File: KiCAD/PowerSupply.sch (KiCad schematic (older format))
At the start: 12 parts, among them J1 USBAB, Q1 3.7A/20V, U1 LM1117-5.0, U2 AP2112K-3.3

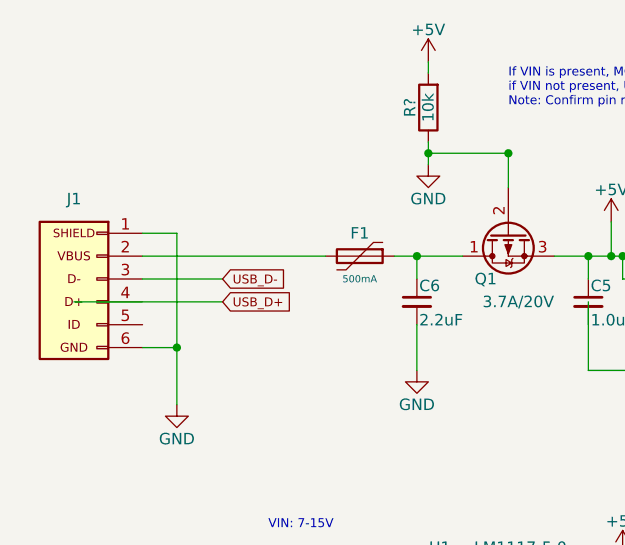
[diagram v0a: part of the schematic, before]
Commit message: Broke out pins from MCU and added data bus protection diode
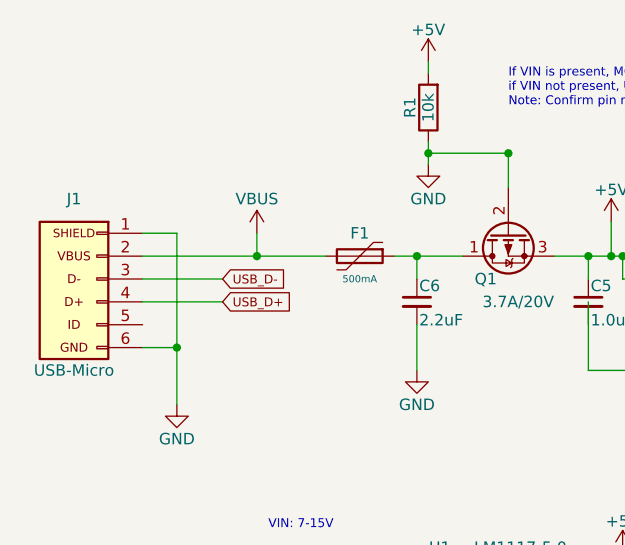
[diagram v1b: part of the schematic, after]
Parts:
- J1: value USBAB -> USB-Micro
- gave numbers to parts that had none: 1
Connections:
- net labels added: VBUS
- wire segments 36 -> 37
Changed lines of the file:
@@
 $EndDescr
 $Comp
-L GND #PWR?
+L GND #PWR201
 U 1 1 5BF271E8
 P 4600 4100
-F 0 "#PWR?" H 4600 3850 50  0001 C CNN
+F 0 "#PWR201" H 4600 3850 50  0001 C CNN
 F 1 "GND" H 4600 3950 50  0000 C CNN
 F 2 "" H 4600 4100 50  0001 C CNN
@@
 $EndComp
 $Comp
-L R R?
+L R R1
 U 1 1 5BF27207
 P 5700 2800
-F 0 "R?" V 5780 2800 50  0000 C CNN
+F 0 "R1" V 5780 2800 50  0000 C CNN
 F 1 "10k" V 5700 2800 50  0000 C CNN
 F 2 "" V 5630 2800 50  0001 C CNN
@@
 $EndComp
 $Comp
-L GND #PWR?
+L GND #PWR205
 U 1 1 5BF2720F
 P 5700 3050
-F 0 "#PWR?" H 5700 2800 50  0001 C CNN
+F 0 "#PWR205" H 5700 2800 50  0001 C CNN
 F 1 "GND" H 5700 2900 50  0000 C CNN
 F 2 "" H 5700 3050 50  0001 C CNN
@@
 VIN
 $Comp
-L +5V #PWR?
+L +5V #PWR204
 U 1 1 5BF27217
 P 5700 2600
-F 0 "#PWR?" H 5700 2450 50  0001 C CNN
+F 0 "#PWR204" H 5700 2450 50  0001 C CNN
 F 1 "+5V" H 5700 2740 50  0000 C CNN
 F 2 "" H 5700 2600 50  0001 C CNN
@@
 P 4150 3550
 F 0 "J1" H 4150 3900 50  0000 C CNN
-F 1 "USBAB" H 4150 3150 50  0001 C CNN
+F 1 "USB-Micro" H 4150 3150 50  0000 C CNN
 F 2 "" H 4250 3550 50  0001 C CNN
 F 3 "" H 4250 3550 50  0001 C CNN
@@
 VIN: 7-15V
 $Comp
-L GND #PWR?
+L GND #PWR206
 U 1 1 5BF27ED3
 P 5900 5250
-F 0 "#PWR?" H 5900 5000 50  0001 C CNN
+F 0 "#PWR206" H 5900 5000 50  0001 C CNN
 F 1 "GND" H 5900 5100 50  0000 C CNN
 F 2 "" H 5900 5250 50  0001 C CNN
@@
 $EndComp
 $Comp
-L +5V #PWR?
+L +5V #PWR208
 U 1 1 5BF285D5
 P 6550 4750
-F 0 "#PWR?" H 6550 4600 50  0001 C CNN
+F 0 "#PWR208" H 6550 4600 50  0001 C CNN
 F 1 "+5V" H 6550 4890 50  0000 C CNN
 F 2 "" H 6550 4750 50  0001 C CNN
@@
 $EndComp
 $Comp
-L GND #PWR?
+L GND #PWR209
 U 1 1 5BF28EA0
 P 6950 3950
-F 0 "#PWR?" H 6950 3700 50  0001 C CNN
+F 0 "#PWR209" H 6950 3700 50  0001 C CNN
 F 1 "GND" H 6950 3800 50  0000 C CNN
 F 2 "" H 6950 3950 50  0001 C CNN
@@
 $EndComp
 $Comp
-L +3.3V #PWR?
+L +3.3V #PWR210
 U 1 1 5BF2913F
 P 7600 3350
-F 0 "#PWR?" H 7600 3200 50  0001 C CNN
+F 0 "#PWR210" H 7600 3200 50  0001 C CNN
 F 1 "+3.3V" H 7600 3490 50  0000 C CNN
 F 2 "" H 7600 3350 50  0001 C CNN
@@
 	1    0    0    -1
 $EndComp
-Wire Wire Line
-	4600 3350 4600 4100
-Wire Wire Line
-	4450 3850 4600 3850
-Wire Wire Line
-	4450 3350 4600 3350
-Connection ~ 4600 3850
-Wire Wire Line
-	4150 3650 4800 3650
-Wire Wire Line
-	4450 3450 5250 3450
-Wire Wire Line
-	5550 3450 5850 3450
-Wire Wire Line
-	6050 3000 6050 3150
-Connection ~ 6050 3000
-Wire Wire Line
-	5700 2950 5700 3050
-Wire Wire Line
-	5700 2650 5700 2600
-Wire Wire Line
-	6050 3000 5700 3000
-Connection ~ 5700 3000
-Wire Wire Line
-	4450 3550 4800 3550
-Wire Wire Line
-	5150 4850 5600 4850
-Wire Wire Line
-	5900 5250 5900 5150
-Wire Wire Line
-	5450 5100 5450 5200
-Wire Wire Line
-	5450 5200 6700 5200
-Connection ~ 5900 5200
-Wire Wire Line
-	5450 4900 5450 4850
-Connection ~ 5450 4850
-Wire Wire Line
-	6400 5200 6400 5100
-Wire Wire Line
-	6200 4850 6700 4850
-Wire Wire Line
-	6400 4850 6400 4900
-Wire Wire Line
-	6700 5200 6700 5100
-Connection ~ 6400 5200
-Wire Wire Line
-	6700 4850 6700 4900
-Connection ~ 6400 4850
-Wire Wire Line
-	6550 4850 6550 4750
-Connection ~ 6550 4850
-Wire Wire Line
-	7250 3450 7750 3450
-Wire Wire Line
-	6950 3950 6950 3850
-Wire Wire Line
-	6400 3950 7750 3950
-Wire Wire Line
-	6250 3450 6650 3450
-Wire Wire Line
-	6650 3550 6550 3550
-Wire Wire Line
-	6550 3550 6550 3450
-Connection ~ 6550 3450
-Wire Wire Line
-	6400 3650 6400 3950
-Connection ~ 6950 3950
-Wire Wire Line
-	7750 3950 7750 3650
-Wire Wire Line
-	7600 3350 7600 3450
-Connection ~ 7600 3450
 $Comp
 L C_Small C6
@@
 	1    0    0    -1
 $EndComp
-Wire Wire Line
-	7750 3450 7750 3550
-Wire Wire Line
-	6400 3550 6400 3450
-Connection ~ 6400 3450
-Wire Wire Line
-	5650 3550 5650 3450
-Connection ~ 5650 3450
-$Comp
-L GND #PWR?
+$Comp
+L GND #PWR203
 U 1 1 5BF29400
 P 5650 3950
-F 0 "#PWR?" H 5650 3700 50  0001 C CNN
+F 0 "#PWR203" H 5650 3700 50  0001 C CNN
 F 1 "GND" H 5650 3800 50  0000 C CNN
 F 2 "" H 5650 3950 50  0001 C CNN
@@
 	1    0    0    -1
 $EndComp
-Wire Wire Line
-	5650 3950 5650 3750
-$Comp
-L +5V #PWR?
+$Comp
+L +5V #PWR207
 U 1 1 5BF2A2B6
 P 6500 3300
-F 0 "#PWR?" H 6500 3150 50  0001 C CNN
+F 0 "#PWR207" H 6500 3150 50  0001 C CNN
 F 1 "+5V" H 6500 3440 50  0000 C CNN
 F 2 "" H 6500 3300 50  0001 C CNN
@@
 	1    0    0    -1
 $EndComp
-Wire Wire Line
-	6500 3300 6500 3450
-Connection ~ 6500 3450
 Text Notes 6050 2800 0    39   ~ 0
 If VIN is present, MOSFET will not conduct\nif VIN not present, USB_VBUS will flow through Q1\nNote: Confirm pin numbering with part
+$Comp
+L VBUS #PWR202
+U 1 1 5BF2FD1D
+P 4950 3350
+F 0 "#PWR202" H 4950 3200 50  0001 C CNN
+F 1 "VBUS" H 4950 3500 50  0000 C CNN
+F 2 "" H 4950 3350 50  0001 C CNN
+F 3 "" H 4950 3350 50  0001 C CNN
+	1    4950 3350
+	1    0    0    -1
+$EndComp
+Wire Wire Line
+	6400 3650 6400 3950
+Connection ~ 4950 3450
+Wire Wire Line
+	4950 3350 4950 3450
+Wire Wire Line
+	4450 3650 4800 3650
+Connection ~ 6500 3450
+Wire Wire Line
+	6500 3300 6500 3450
+Wire Wire Line
+	5650 3950 5650 3750
+Connection ~ 5650 3450
+Wire Wire Line
+	5650 3550 5650 3450
+Connection ~ 6400 3450
+Wire Wire Line
+	6400 3550 6400 3450
+Wire Wire Line
+	7750 3450 7750 3550
+Connection ~ 7600 3450
+Wire Wire Line
+	7600 3350 7600 3450
+Wire Wire Line
+	7750 3950 7750 3650
+Connection ~ 6950 3950
+Connection ~ 6550 3450
+Wire Wire Line
+	6550 3550 6550 3450
+Wire Wire Line
+	6650 3550 6550 3550
+Wire Wire Line
+	6250 3450 6650 3450
+Wire Wire Line
+	6400 3950 7750 3950
+Wire Wire Line
+	6950 3950 6950 3850
+Wire Wire Line
+	7250 3450 7750 3450
+Connection ~ 6550 4850
+Wire Wire Line
+	6550 4850 6550 4750
+Connection ~ 6400 4850
+Wire Wire Line
+	6700 4850 6700 4900
+Connection ~ 6400 5200
+Wire Wire Line
+	6700 5200 6700 5100
+Wire Wire Line
+	6400 4850 6400 4900
+Wire Wire Line
+	6200 4850 6700 4850
+Wire Wire Line
+	6400 5200 6400 5100
+Connection ~ 5450 4850
+Wire Wire Line
+	5450 4900 5450 4850
+Connection ~ 5900 5200
+Wire Wire Line
+	5450 5200 6700 5200
+Wire Wire Line
+	5450 5100 5450 5200
+Wire Wire Line
+	5900 5250 5900 5150
+Wire Wire Line
+	5150 4850 5600 4850
+Wire Wire Line
+	4450 3550 4800 3550
+Connection ~ 5700 3000
+Wire Wire Line
+	6050 3000 5700 3000
+Wire Wire Line
+	5700 2650 5700 2600
+Wire Wire Line
+	5700 2950 5700 3050
+Connection ~ 6050 3000
+Wire Wire Line
+	6050 3000 6050 3150
+Wire Wire Line
+	5550 3450 5850 3450
+Wire Wire Line
+	4450 3450 5250 3450
+Connection ~ 4600 3850
+Wire Wire Line
+	4450 3350 4600 3350
+Wire Wire Line
+	4450 3850 4600 3850
+Wire Wire Line
+	4600 3350 4600 4100
 $EndSCHEMATC

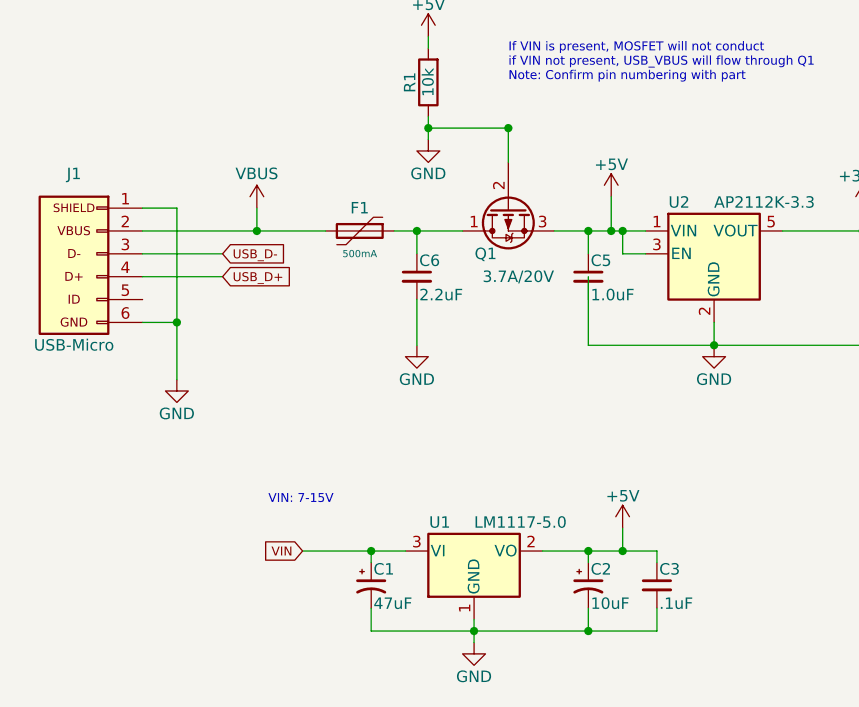
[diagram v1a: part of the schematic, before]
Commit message: Editing capacitor values, prepping for layout phase
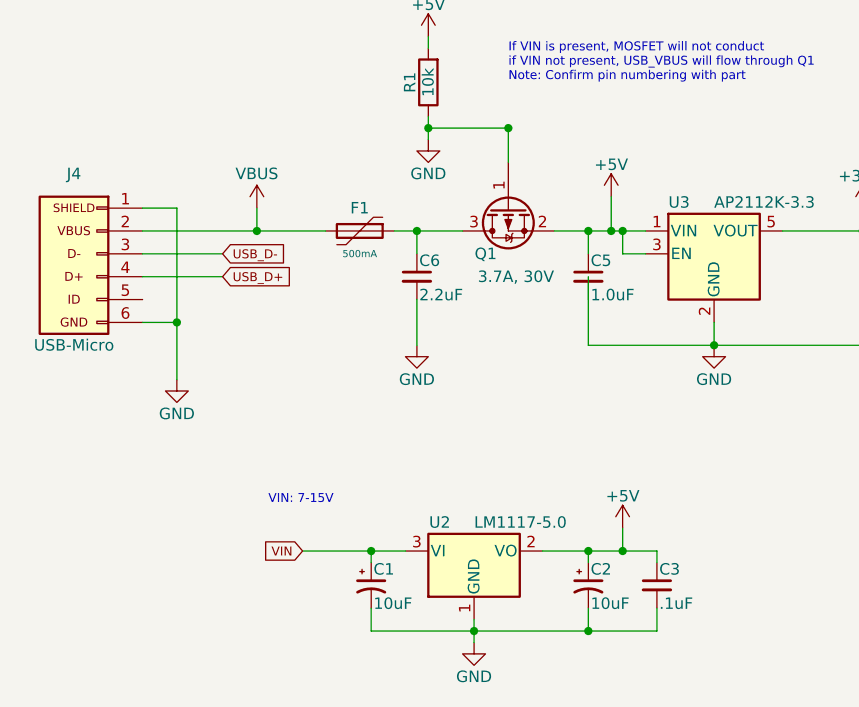
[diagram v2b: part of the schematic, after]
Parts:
- removed Q1: 3.7A/20V, symbol Q_PMOS_DGS
- added Q1: 3.7A, 30V, symbol Q_PMOS_GSD
- C1: value 47uF -> 10uF
- renumbered J1 to J4, U1 to U2, U2 to U3
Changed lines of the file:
@@
 LIBS:MF-MSMF050-2
 LIBS:AP2112K-3.3TRG1
+LIBS:cortex_debug
+LIBS:B3FS-4005P
 LIBS:SAMD21-DevBoard-cache
 EELAYER 25 0
@@
 $EndComp
 $Comp
-L Q_PMOS_DGS Q1
-U 1 1 5BF271FF
-P 6050 3350
-F 0 "Q1" V 6250 3400 50  0000 L CNN
-F 1 "3.7A/20V" V 6350 3150 50  0000 L CNN
-F 2 "" H 6250 3450 50  0001 C CNN
-F 3 "" H 6050 3350 50  0001 C CNN
-	1    6050 3350
-	0    -1   1    0
-$EndComp
-$Comp
 L R R1
 U 1 1 5BF27207
@@
 $EndComp
 $Comp
-L USBAB J1
+L USBAB J4
 U 1 1 5BF271E1
 P 4150 3550
-F 0 "J1" H 4150 3900 50  0000 C CNN
+F 0 "J4" H 4150 3900 50  0000 C CNN
 F 1 "USB-Micro" H 4150 3150 50  0000 C CNN
 F 2 "" H 4250 3550 50  0001 C CNN
@@
 $EndComp
 $Comp
-L LM1117-5.0 U1
+L LM1117-5.0 U2
 U 1 1 5BF2791A
 P 5900 4850
-F 0 "U1" H 5750 4975 50  0000 C CNN
+F 0 "U2" H 5750 4975 50  0000 C CNN
 F 1 "LM1117-5.0" H 5900 4975 50  0000 L CNN
 F 2 "" H 5900 4850 50  0001 C CNN
@@
 P 5450 5000
 F 0 "C1" H 5460 5070 50  0000 L CNN
-F 1 "47uF" H 5460 4920 50  0000 L CNN
+F 1 "10uF" H 5460 4920 50  0000 L CNN
 F 2 "" H 5450 5000 50  0001 C CNN
 F 3 "" H 5450 5000 50  0001 C CNN
@@
 $EndComp
 $Comp
-L AP2112K-3.3 U2
+L AP2112K-3.3 U3
 U 1 1 5BF28D97
 P 6950 3550
-F 0 "U2" H 6750 3775 50  0000 L CNN
+F 0 "U3" H 6750 3775 50  0000 L CNN
 F 1 "AP2112K-3.3" H 6950 3775 50  0000 L CNN
 F 2 "TO_SOT_Packages_SMD:SOT-23-5" H 6950 3875 50  0001 C CNN
@@
 Wire Wire Line
 	4600 3350 4600 4100
+$Comp
+L Q_PMOS_GSD Q1
+U 1 1 5C02D8EB
+P 6050 3350
+F 0 "Q1" V 6250 3400 50  0000 L CNN
+F 1 "3.7A, 30V" V 6350 3150 50  0000 L CNN
+F 2 "" H 6250 3450 50  0001 C CNN
+F 3 "" H 6050 3350 50  0001 C CNN
+	1    6050 3350
+	0    -1   1    0
+$EndComp
 $EndSCHEMATC

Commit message: Created footprints for switch, micro usb port and crystal
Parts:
- C1, C2, C3: footprint (none) -> Capacitors_SMD:C_1206
- C4, C5, C6: footprint (none) -> Capacitors_SMD:C_1210
- F1, R1: footprint (none) -> Resistors_SMD:R_1210
- J4: footprint (none) -> 10118192-0001LF:10118192-0001LF
- Q1: footprint (none) -> TO_SOT_Packages_SMD:SOT-23
- U2: footprint (none) -> TO_SOT_Packages_SMD:SOT-223
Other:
- note added: "0"
- note added: "12/2/18"
- note added: "Author: Matthew Cox\nOrganization: University of Connecticut Formula SAE"
- note added: "If VIN is present, MOSFET will not conduct\nif VIN not present, USB_VBUS will flow through Q1"
- note added: "SAMD21 Dev Board - Power Supply"
- note removed: "If VIN is present, MOSFET will not conduct\nif VIN not present, USB_VBUS will flow through Q1\nNote: Confirm pin numbering with part"
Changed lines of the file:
@@
 $EndDescr
 $Comp
-L GND #PWR201
+L GND #PWR027
 U 1 1 5BF271E8
-P 4600 4100
-F 0 "#PWR201" H 4600 3850 50  0001 C CNN
-F 1 "GND" H 4600 3950 50  0000 C CNN
-F 2 "" H 4600 4100 50  0001 C CNN
-F 3 "" H 4600 4100 50  0001 C CNN
-	1    4600 4100
+P 4600 3950
+F 0 "#PWR027" H 4600 3700 50  0001 C CNN
+F 1 "GND" H 4600 3800 50  0000 C CNN
+F 2 "" H 4600 3950 50  0001 C CNN
+F 3 "" H 4600 3950 50  0001 C CNN
+	1    4600 3950
 	1    0    0    -1
 $EndComp
@@
 F 0 "F1" V 5300 3450 50  0000 C CNN
 F 1 "500mA" V 5500 3450 31  0000 C CNN
-F 2 "" H 5450 3250 50  0001 L CNN
+F 2 "Resistors_SMD:R_1210" H 5450 3250 50  0001 L CNN
 F 3 "" H 5400 3450 50  0001 C CNN
 	1    5400 3450
@@
 F 0 "R1" V 5780 2800 50  0000 C CNN
 F 1 "10k" V 5700 2800 50  0000 C CNN
-F 2 "" V 5630 2800 50  0001 C CNN
+F 2 "Resistors_SMD:R_1210" V 5630 2800 50  0001 C CNN
 F 3 "" H 5700 2800 50  0001 C CNN
 	1    5700 2800
@@
 $EndComp
 $Comp
-L GND #PWR205
+L GND #PWR028
 U 1 1 5BF2720F
 P 5700 3050
-F 0 "#PWR205" H 5700 2800 50  0001 C CNN
+F 0 "#PWR028" H 5700 2800 50  0001 C CNN
 F 1 "GND" H 5700 2900 50  0000 C CNN
 F 2 "" H 5700 3050 50  0001 C CNN
@@
 VIN
 $Comp
-L +5V #PWR204
+L +5V #PWR029
 U 1 1 5BF27217
 P 5700 2600
-F 0 "#PWR204" H 5700 2450 50  0001 C CNN
+F 0 "#PWR029" H 5700 2450 50  0001 C CNN
 F 1 "+5V" H 5700 2740 50  0000 C CNN
 F 2 "" H 5700 2600 50  0001 C CNN
@@
 F 0 "J4" H 4150 3900 50  0000 C CNN
 F 1 "USB-Micro" H 4150 3150 50  0000 C CNN
-F 2 "" H 4250 3550 50  0001 C CNN
+F 2 "10118192-0001LF:10118192-0001LF" H 4250 3550 50  0001 C CNN
 F 3 "" H 4250 3550 50  0001 C CNN
 	1    4150 3550
@@
 F 0 "U2" H 5750 4975 50  0000 C CNN
 F 1 "LM1117-5.0" H 5900 4975 50  0000 L CNN
-F 2 "" H 5900 4850 50  0001 C CNN
+F 2 "TO_SOT_Packages_SMD:SOT-223" H 5900 4850 50  0001 C CNN
 F 3 "" H 5900 4850 50  0001 C CNN
 	1    5900 4850
@@
 VIN: 7-15V
 $Comp
-L GND #PWR206
+L GND #PWR030
 U 1 1 5BF27ED3
 P 5900 5250
-F 0 "#PWR206" H 5900 5000 50  0001 C CNN
+F 0 "#PWR030" H 5900 5000 50  0001 C CNN
 F 1 "GND" H 5900 5100 50  0000 C CNN
 F 2 "" H 5900 5250 50  0001 C CNN
@@
 F 0 "C1" H 5460 5070 50  0000 L CNN
 F 1 "10uF" H 5460 4920 50  0000 L CNN
-F 2 "" H 5450 5000 50  0001 C CNN
+F 2 "Capacitors_SMD:C_1206" H 5450 5000 50  0001 C CNN
 F 3 "" H 5450 5000 50  0001 C CNN
 	1    5450 5000
@@
 F 0 "C2" H 6410 5070 50  0000 L CNN
 F 1 "10uF" H 6410 4920 50  0000 L CNN
-F 2 "" H 6400 5000 50  0001 C CNN
+F 2 "Capacitors_SMD:C_1206" H 6400 5000 50  0001 C CNN
 F 3 "" H 6400 5000 50  0001 C CNN
 	1    6400 5000
@@
 F 0 "C3" H 6710 5070 50  0000 L CNN
 F 1 ".1uF" H 6710 4920 50  0000 L CNN
-F 2 "" H 6700 5000 50  0001 C CNN
+F 2 "Capacitors_SMD:C_1206" H 6700 5000 50  0001 C CNN
 F 3 "" H 6700 5000 50  0001 C CNN
 	1    6700 5000
@@
 $EndComp
 $Comp
-L +5V #PWR208
+L +5V #PWR031
 U 1 1 5BF285D5
 P 6550 4750
-F 0 "#PWR208" H 6550 4600 50  0001 C CNN
+F 0 "#PWR031" H 6550 4600 50  0001 C CNN
 F 1 "+5V" H 6550 4890 50  0000 C CNN
 F 2 "" H 6550 4750 50  0001 C CNN
@@
 F 0 "C4" H 7760 3720 50  0000 L CNN
 F 1 "2.2uF" H 7760 3570 50  0000 L CNN
-F 2 "" H 7750 3650 50  0001 C CNN
+F 2 "Capacitors_SMD:C_1210" H 7750 3650 50  0001 C CNN
 F 3 "" H 7750 3650 50  0001 C CNN
 	1    7750 3650
@@
 $EndComp
 $Comp
-L GND #PWR209
+L GND #PWR032
 U 1 1 5BF28EA0
 P 6950 3950
-F 0 "#PWR209" H 6950 3700 50  0001 C CNN
+F 0 "#PWR032" H 6950 3700 50  0001 C CNN
 F 1 "GND" H 6950 3800 50  0000 C CNN
 F 2 "" H 6950 3950 50  0001 C CNN
@@
 F 0 "C5" H 6410 3720 50  0000 L CNN
 F 1 "1.0uF" H 6410 3570 50  0000 L CNN
-F 2 "" H 6400 3650 50  0001 C CNN
+F 2 "Capacitors_SMD:C_1210" H 6400 3650 50  0001 C CNN
 F 3 "" H 6400 3650 50  0001 C CNN
 	1    6400 3650
@@
 $EndComp
 $Comp
-L +3.3V #PWR210
+L +3.3V #PWR033
 U 1 1 5BF2913F
 P 7600 3350
-F 0 "#PWR210" H 7600 3200 50  0001 C CNN
+F 0 "#PWR033" H 7600 3200 50  0001 C CNN
 F 1 "+3.3V" H 7600 3490 50  0000 C CNN
 F 2 "" H 7600 3350 50  0001 C CNN
@@
 F 0 "C6" H 5660 3720 50  0000 L CNN
 F 1 "2.2uF" H 5660 3570 50  0000 L CNN
-F 2 "" H 5650 3650 50  0001 C CNN
+F 2 "Capacitors_SMD:C_1210" H 5650 3650 50  0001 C CNN
 F 3 "" H 5650 3650 50  0001 C CNN
 	1    5650 3650
@@
 $EndComp
 $Comp
-L GND #PWR203
+L GND #PWR034
 U 1 1 5BF29400
 P 5650 3950
-F 0 "#PWR203" H 5650 3700 50  0001 C CNN
+F 0 "#PWR034" H 5650 3700 50  0001 C CNN
 F 1 "GND" H 5650 3800 50  0000 C CNN
 F 2 "" H 5650 3950 50  0001 C CNN
@@
 $EndComp
 $Comp
-L +5V #PWR207
+L +5V #PWR035
 U 1 1 5BF2A2B6
 P 6500 3300
-F 0 "#PWR207" H 6500 3150 50  0001 C CNN
+F 0 "#PWR035" H 6500 3150 50  0001 C CNN
 F 1 "+5V" H 6500 3440 50  0000 C CNN
 F 2 "" H 6500 3300 50  0001 C CNN
@@
 $EndComp
 Text Notes 6050 2800 0    39   ~ 0
-If VIN is present, MOSFET will not conduct\nif VIN not present, USB_VBUS will flow through Q1\nNote: Confirm pin numbering with part
-$Comp
-L VBUS #PWR202
+If VIN is present, MOSFET will not conduct\nif VIN not present, USB_VBUS will flow through Q1
+$Comp
+L VBUS #PWR036
 U 1 1 5BF2FD1D
 P 4950 3350
-F 0 "#PWR202" H 4950 3200 50  0001 C CNN
+F 0 "#PWR036" H 4950 3200 50  0001 C CNN
 F 1 "VBUS" H 4950 3500 50  0000 C CNN
 F 2 "" H 4950 3350 50  0001 C CNN
@@
 	1    0    0    -1
 $EndComp
-Wire Wire Line
-	6400 3650 6400 3950
 Connection ~ 4950 3450
 Wire Wire Line
@@
 Wire Wire Line
 	7600 3350 7600 3450
-Wire Wire Line
-	7750 3950 7750 3650
 Connection ~ 6950 3950
 Connection ~ 6550 3450
@@
 Wire Wire Line
 	4450 3850 4600 3850
-Wire Wire Line
-	4600 3350 4600 4100
 $Comp
 L Q_PMOS_GSD Q1
@@
 F 0 "Q1" V 6250 3400 50  0000 L CNN
 F 1 "3.7A, 30V" V 6350 3150 50  0000 L CNN
-F 2 "" H 6250 3450 50  0001 C CNN
+F 2 "TO_SOT_Packages_SMD:SOT-23" H 6250 3450 50  0001 C CNN
 F 3 "" H 6050 3350 50  0001 C CNN
 	1    6050 3350
 	0    -1   1    0
 $EndComp
+Wire Wire Line
+	4600 3350 4600 3950
+Wire Wire Line
+	6400 3950 6400 3750
+Wire Wire Line
+	7750 3950 7750 3750
+Text Notes 7400 7500 0    47   ~ 0
+SAMD21 Dev Board - Power Supply
+Text Notes 8200 7650 0    47   ~ 0
+12/2/18
+Text Notes 10600 7650 0    47   ~ 0
+0
+Text Notes 7000 7100 0    79   ~ 0
+Author: Matthew Cox\nOrganization: University of Connecticut Formula SAE
 $EndSCHEMATC

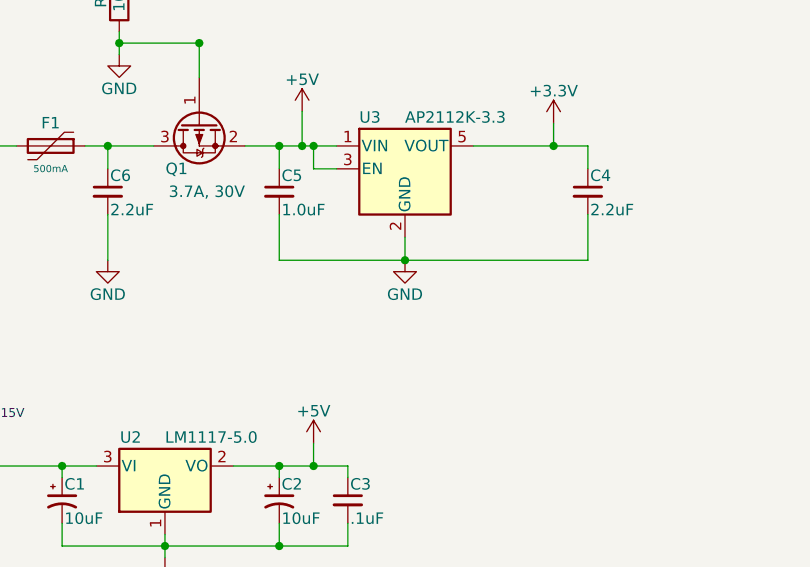
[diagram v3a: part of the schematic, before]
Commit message: Generate netlist and begin layout
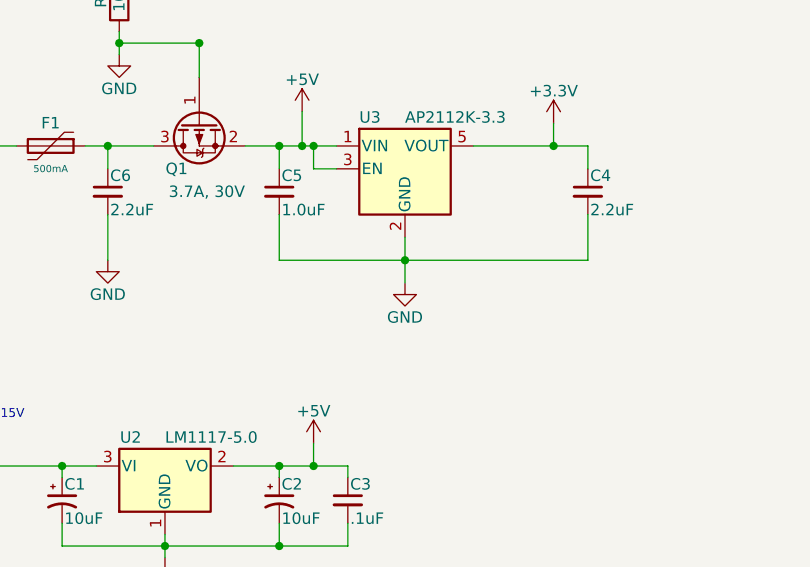
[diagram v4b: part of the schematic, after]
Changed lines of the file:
@@
 L GND #PWR032
 U 1 1 5BF28EA0
-P 6950 3950
-F 0 "#PWR032" H 6950 3700 50  0001 C CNN
-F 1 "GND" H 6950 3800 50  0000 C CNN
-F 2 "" H 6950 3950 50  0001 C CNN
-F 3 "" H 6950 3950 50  0001 C CNN
-	1    6950 3950
+P 6950 4050
+F 0 "#PWR032" H 6950 3800 50  0001 C CNN
+F 1 "GND" H 6950 3900 50  0000 C CNN
+F 2 "" H 6950 4050 50  0001 C CNN
+F 3 "" H 6950 4050 50  0001 C CNN
+	1    6950 4050
 	1    0    0    -1
 $EndComp
@@
 	6400 3950 7750 3950
 Wire Wire Line
-	6950 3950 6950 3850
+	6950 3850 6950 4050
 Wire Wire Line
 	7250 3450 7750 3450
